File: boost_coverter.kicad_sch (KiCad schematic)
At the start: 21 parts, among them Q201 AO3401A, U201 TPS65131RGE

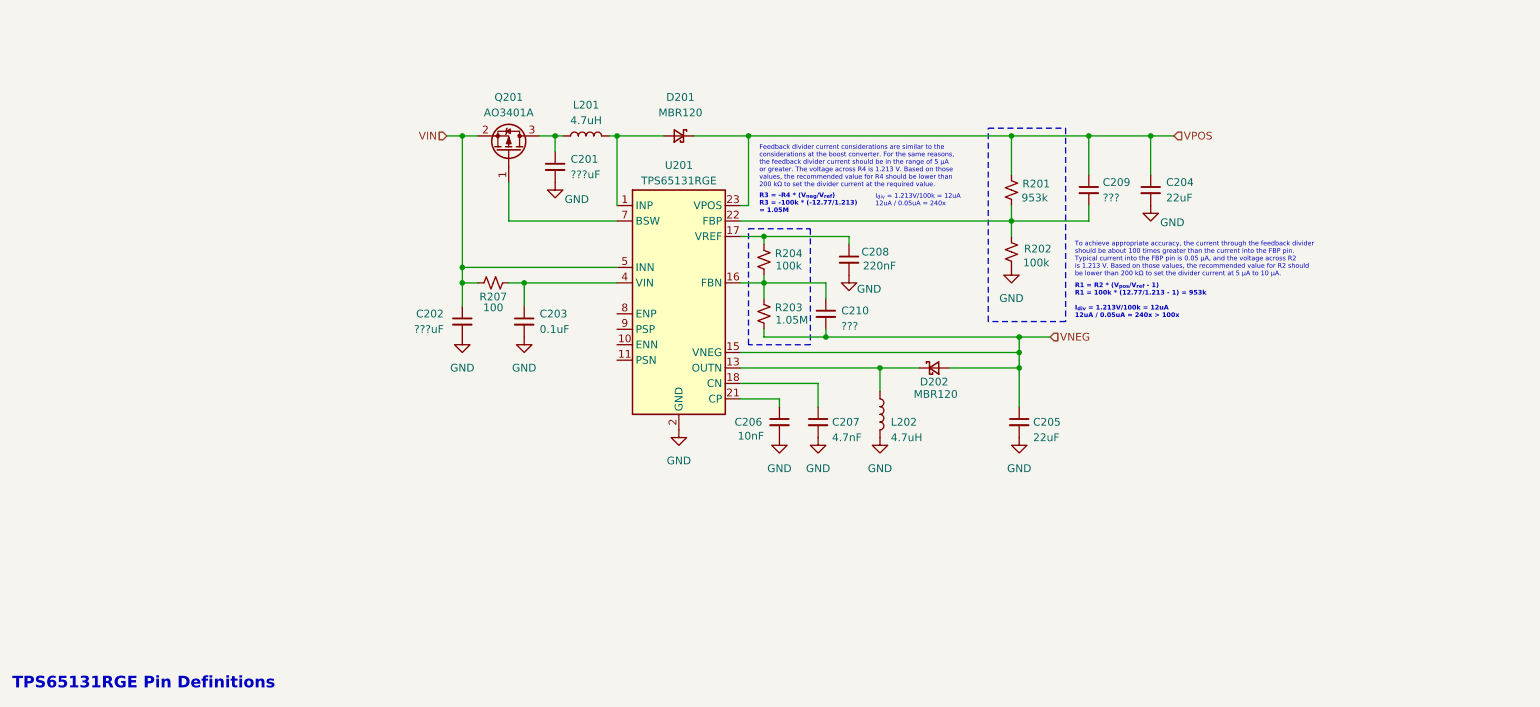
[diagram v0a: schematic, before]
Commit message: Finished TPS65131 schematic.
Finalized inductor and capacitor calculations. Exposed EN pin with pull-downs for default off state. Disabled low-power/burst mode.
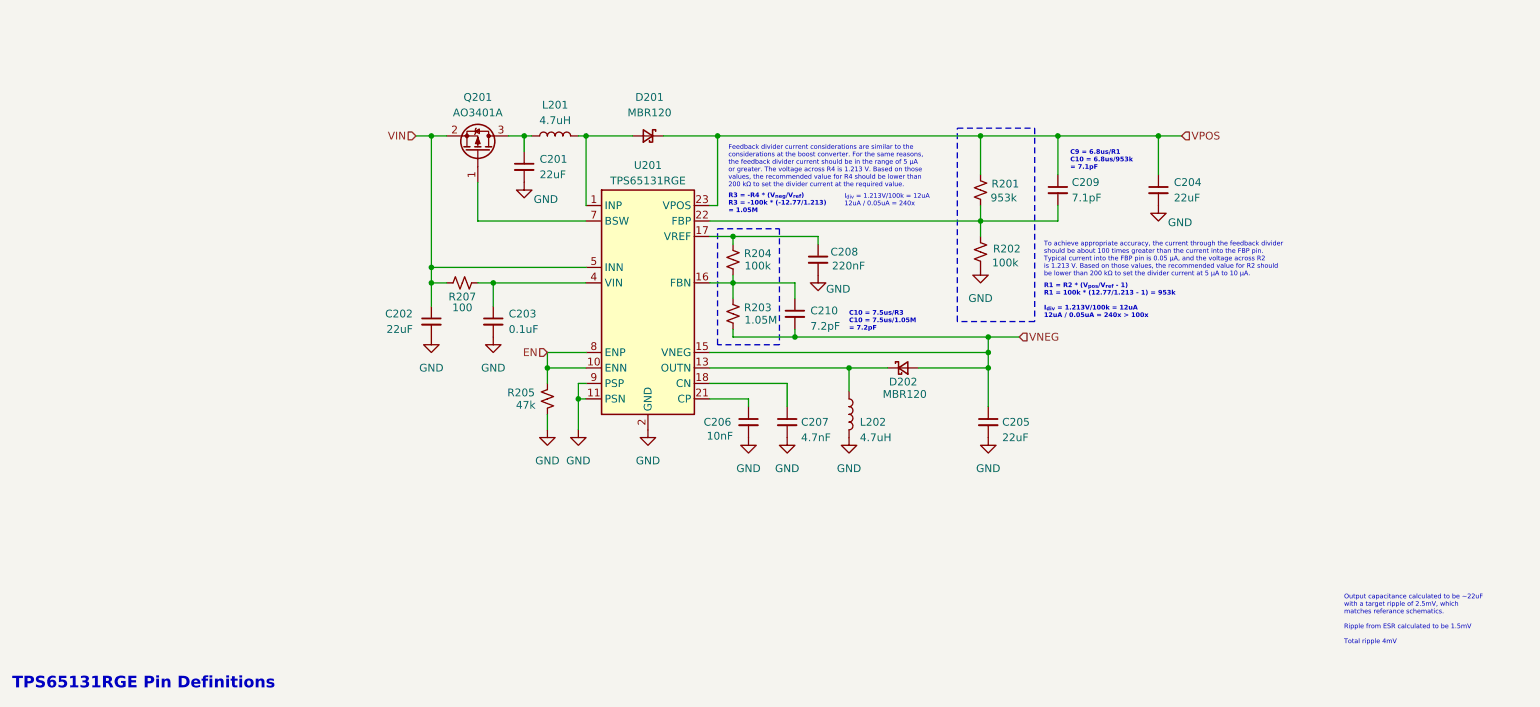
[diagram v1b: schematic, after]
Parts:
- added R205: 47k, symbol Device:R_Small_US
- C201, C202: value ???uF -> 22uF
- C209: value ??? -> 7.1pF
- C210: value ??? -> 7.2pF
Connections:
- net GND: now also U201.11 (PSN), U201.9 (PSP), R205.1
- net EN: now reaches U201.10 (ENN)
- net EN: now also U201.8 (ENP), R205.2
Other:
- note added: "C10 = 7.5us/R3 C10 = 7.5us/1.05M = 7.2pF"
- note added: "C9 = 6.8us/R1 C10 = 6.8us/953k = 7.1pF"
- note added: "Output capacitance calculated to be ~22uF with a target ripple of 2.5mV, which matches referance schematics. Ripple from ESR calculated to be 1.5mV Total ripple 4mV"
- moved on the sheet: C201, C202, C203, C204, C205, C206, C207, C208, C209, C210, D201, D202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

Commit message: Annotated Boost Schematic
Beware of typos
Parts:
- added R206: 47k, symbol Device:R_Small_US
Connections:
- net EN: now also R206.1
- net VIN: no longer U201.6 (INN)
- net at C203.1, R207.2, U201.4 (VIN): now also R206.2
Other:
- note added: "-12.77V"
- note added: "12.77V"
- note added: "An input bulk capacitor of at least 4.7 uF is recommended to improve transient response. A value of 22 uF was selected for both the INP and INN capacitors to improve performance when powered from a potentially unstable USB source. A 0.1 uF ceramic bypass capacitor should be placed close to the VIN pin."
- note added: "An output capacitance of 22uF matches reference schematics, which results in a voltage ripple of 2.3mV. ESR of 1.5R * Output Current of 100mA = additional 1.5mV Ripple"
- note added: "An output capacitance of 22uF matches reference schematics, which results in a voltage ripple of 2.5mV. ESR of 1.5R * Output Current of 100mA = additional 1.5mV Ripple"
- note added: "Because the TPS65131 is designed to use inductors between 3.3 uH and 6.8 uH, the recommended 4.7 uH inductor was selected. Based on the provided calculations, the positive inductor ripple current will be 0.52 of I_{LP}. While this is higher than the recommended 20%, this is expected due to the low output current of 100 mA."
- note added: "C4_{min} = I_{POS}*(V_{POS} - V_{I}) / f * ΔV_{POS} * V_{POS} C4_{min} = 100mA *(12.77V - 5V) / 1.25MHz * 2.5mV * 12.77V C4_{min} = 19uF"
- note added: "C5_{min} = I_{NEG}*V_{NEG} / f * ΔV_{NEG} * (V_{NEG} - V{I}) C5_{min} = 100mA * -12.77V / 1.25MHz * 2.5mV * (-12.77V - 5V) C5_{min} = 22uF"
- note added: "ENP and ENN tied together and exposed via EN pin to allow MCU control over PSU."
- note added: "Feedforward Capacitor"
- note added: "PSP ON = PSP OFF = ~83% @ 100mA PSN ON = PSN OFF = ~82% @ 100mA"
- note added: "Power-Save (Burst Mode) disabled to reduce output ripple magnitude and because efficiency is identical at ~100mA output current."
- note added: "Pulled LOW via a 47 k resistor to set the default state to OFF. An optional pull-up resistor (R6) allows manual control."
- note added: "See annotation on positive inductor at top of sheet."
- note added: "The negative output capacitor value (C5) can be calculated as follows, where ΔV_{NEG} is the maximum allowed output ripple and f is the switching frequency."
- note added: "The positive output capacitor value (C4) can be calculated as follows, where ΔV_{POS} is the maximum allowed output ripple and f is the switching frequency."
- note removed: "Output capacitance calculated to be ~22uF with a target ripple of 2.5mV, which matches referance schematics. Ripple from ESR calculated to be 1.5mV Total ripple 4mV"
- moved on the sheet: C201, C202, C203, C204, C205, C206, C207, C208, C209, C210, D201, D202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

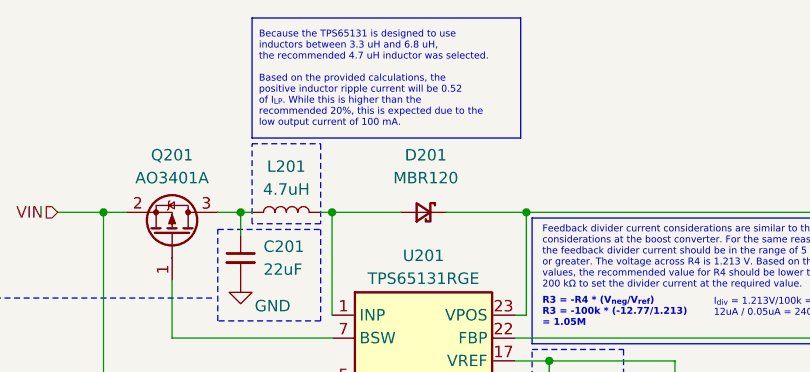
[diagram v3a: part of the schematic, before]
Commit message: MCU LDO & Inputs
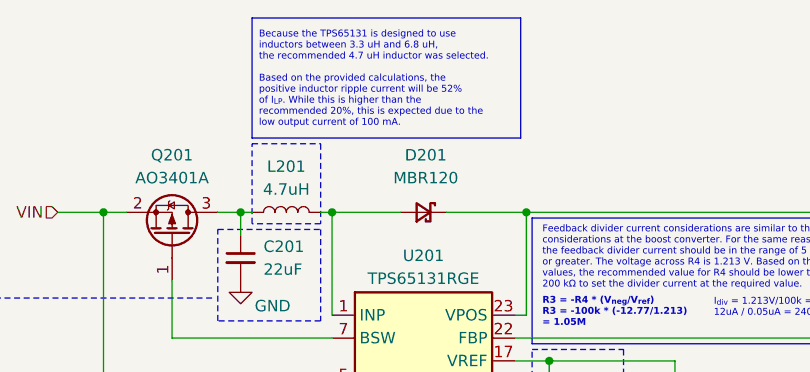
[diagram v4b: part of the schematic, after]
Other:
- note added: "Because the TPS65131 is designed to use inductors between 3.3 uH and 6.8 uH, the recommended 4.7 uH inductor was selected. Based on the provided calculations, the positive inductor ripple current will be 52% of I_{LP}. While this is higher than the recommended 20%, this is expected due to the low output current of 100 mA."
- note removed: "Because the TPS65131 is designed to use inductors between 3.3 uH and 6.8 uH, the recommended 4.7 uH inductor was selected. Based on the provided calculations, the positive inductor ripple current will be 0.52 of I_{LP}. While this is higher than the recommended 20%, this is expected due to the low output current of 100 mA."
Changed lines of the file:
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@@
 		)
 	)
-	(text "Because the TPS65131 is designed to use\ninductors between 3.3 uH and 6.8 uH,\nthe recommended 4.7 uH inductor was selected.\n\nBased on the provided calculations, the\npositive inductor ripple current will be 0.52\nof I_{LP}. While this is higher than the\nrecommended 20%, this is expected due to the\nlow output current of 100 mA."
+	(text "Because the TPS65131 is designed to use\ninductors between 3.3 uH and 6.8 uH,\nthe recommended 4.7 uH inductor was selected.\n\nBased on the provided calculations, the\npositive inductor ripple current will be 52%\nof I_{LP}. While this is higher than the\nrecommended 20%, this is expected due to the\nlow output current of 100 mA."
 		(exclude_from_sim no)
 		(at 94.742 37.338 0)

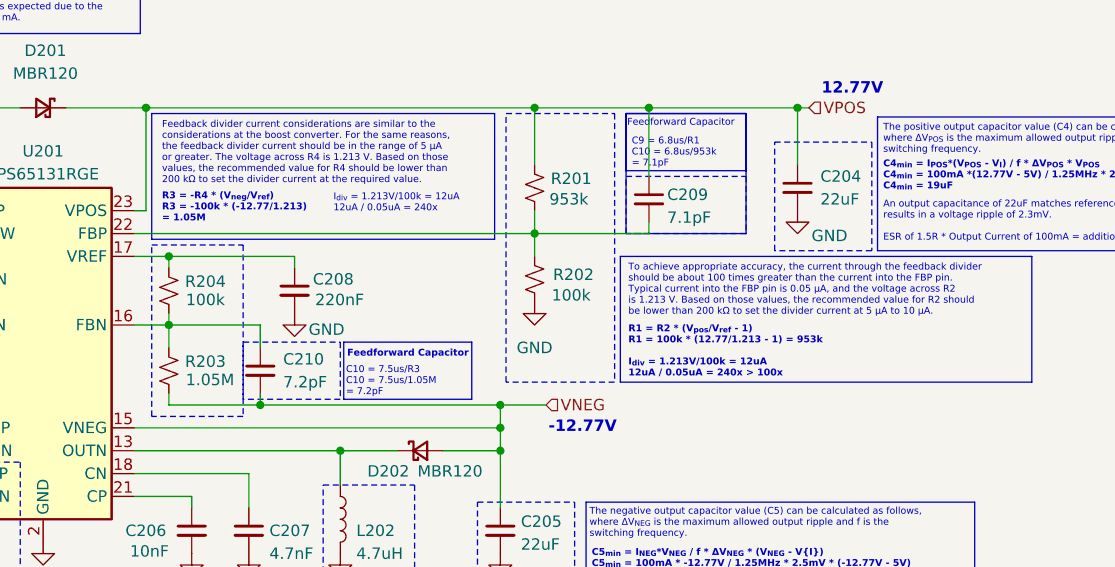
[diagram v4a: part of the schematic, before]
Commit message: Moved VBUS TVS
put VBUS TVS before any other components. Added notes about VBUS soft start and necessity of pi filter
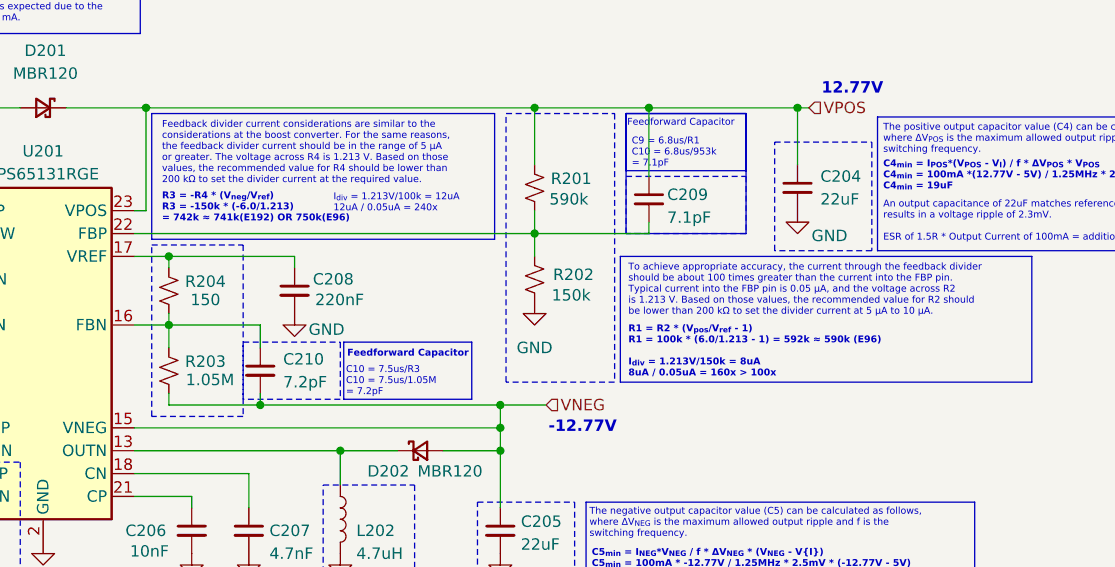
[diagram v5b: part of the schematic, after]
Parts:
- R201: value 953k -> 590k
- R202: value 100k -> 150k
- R204: value 100k -> 150
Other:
- note added: "R1 = R2 * (V_{pos}/V_{ref} - 1) R1 = 100k * (6.0/1.213 - 1) = 592k ≈ 590k (E96) I_{div} = 1.213V/150k = 8uA 8uA / 0.05uA = 160x > 100x"
- note added: "R3 = -R4 * (V_{neg}/V_{ref}) R3 = -150k * (-6.0/1.213) = 742k ≈ 741k(E192) OR 750k(E96)"
- note removed: "R1 = R2 * (V_{pos}/V_{ref} - 1) R1 = 100k * (12.77/1.213 - 1) = 953k I_{div} = 1.213V/100k = 12uA 12uA / 0.05uA = 240x > 100x"
- note removed: "R3 = -R4 * (V_{neg}/V_{ref}) R3 = -100k * (-12.77/1.213) = 1.05M"
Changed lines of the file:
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@@
 		)
 	)
-	(text "R1 = R2 * (V_{pos}/V_{ref} - 1)\nR1 = 100k * (12.77/1.213 - 1) = 953k\n\nI_{div} = 1.213V/100k = 12uA\n12uA / 0.05uA = 240x > 100x"
+	(text "R1 = R2 * (V_{pos}/V_{ref} - 1)\nR1 = 100k * (6.0/1.213 - 1) = 592k ≈ 590k (E96)\n\nI_{div} = 1.213V/150k = 8uA\n8uA / 0.05uA = 160x > 100x"
 		(exclude_from_sim no)
 		(at 178.054 79.248 0)
@@
 		)
 	)
-	(text "R3 = -R4 * (V_{neg}/V_{ref})\nR3 = -100k * (-12.77/1.213)\n= 1.05M"
+	(text "R3 = -R4 * (V_{neg}/V_{ref})\nR3 = -150k * (-6.0/1.213)\n= 742k ≈ 741k(E192) OR 750k(E96)"
 		(exclude_from_sim no)
 		(at 126.238 63.246 0)
@@
 			)
 		)
-		(property "Value" "100k"
+		(property "Value" "150k"
 			(at 171.704 72.898 0)
 			(effects
@@
 			)
 		)
-		(property "Value" "953k"
+		(property "Value" "590k"
 			(at 171.45 62.23 0)
 			(effects
@@
 			)
 		)
-		(property "Value" "100k"
+		(property "Value" "150"
 			(at 131.064 73.406 0)
 			(effects
